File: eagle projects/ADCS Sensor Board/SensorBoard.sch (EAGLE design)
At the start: 129 parts, among them Q3 CSTCR4M00G15L99, Q5 32.768kHz, U10 LMV321, U2 ADS7841E_2K5, U3 LMV321, U5 ADS7841E_2K5, U6 REF194GSZ-REEL7, U7 TLV9054IDR, U8 LMV321

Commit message: Buncha layout done
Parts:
- removed C40: 9.1p, rcl:C-EUC0603
- removed C41, C43, C45, C46, C53, C54: 0.1u, rcl:C-EUC0603
- removed C42, C44: 1u, rcl:C-EUC0603
- removed R53, R57, R58: 5.1M, rcl:R-US_R0603
- removed R54, R55: 698k, rcl:R-US_R0603
- removed R59, R60: 10k, rcl:R-US_R0402
- removed R67, R68: 5.6k, rcl:R-US_R0805
- removed R69, R70: 1k, rcl:R-US_R0805
- removed R71, R72: 1.37M, rcl:R-US_R0805
- removed U$11: HMC1053, my_library:HMC1053
- removed U$14: LM20BIM7X_NOPB, my_library:LM20BIM7X_NOPB
- removed U$3: MTI-1, my_library:MTI-1
- removed U$7, U$9: BSS138PS,115, my_library:BSS138PS,115
- removed U10: LMV321, my_library:LMV321
- added A1: HMC1053PA0242, my_library:HMC1053PA0242
- added C13, C19, C23, C30: 0.1u, rcl:C-EUC0603
- added C20, C24, C27: 1n, rcl:C-EUC0805
- added C28: 470n, rcl:C-EUC0805
- added C29: 4.7u, rcl:C-EUC0603
- added J6: MTI-1_8428-11B1-RK-TP, my_library:MTI-1_8428-11B1-RK-TP
- added R1: 0R, rcl:R-US_R0402
- added R15: 5.1M, resistor:R-US_R1206
- added R16, R9: 5.6k, rcl:R-US_R0805
- added R2: 47k, rcl:R-US_R0402
- added R27: 27R, rcl:R-US_R0805
- added R28: 10k, rcl:R-US_R0402
- added R3: 1k4, rcl:R-US_R0402
- added R35: 698k, rcl:R-US_R0603
- added R4: 100R, rcl:R-US_R0402
- added R5: 1M, rcl:R-US_R0402
- added R6: 200R, resistor:R-US_R1206
- added R7: 1k, rcl:R-US_R0805
- added U4: LMV321, my_library:LMV321
- added U9: ADS7841E_2K5, my_library:ADS7841E_2K5
- added Y1: 32.768kHz, my_library:MS3V-T1R
- added Y2: CSTCR4M00G15L99, my_library:CSTCR4M00G15L996M00G53Z
- C14: value 470n -> 0.1u; device rcl:C-EUC0805 -> rcl:C-EUC0603
- C17, C25: value 1n -> 0.1u; device rcl:C-EUC0805 -> rcl:C-EUC0603
- C21: device rcl:C-EUC0805 -> resistor:C-EUC1206
- C31: value 1n -> 9.1p; device resistor:C-EUC1206 -> rcl:C-EUC0603
- C32, C33: value 0.1u -> 9.1p
- C34: value 0.1u -> 1u
- C36: value 4.7u -> 1u
- C38, C39: value 9.1p -> 0.1u
- JP1: value 5034801000 -> (none); device my_library:5034801000 -> jumper:JP1Q
- JP2: device jumper:JP1Q -> pinhead:PINHD-2X5
- JP3, JP4: value 5034801000 -> (none); device my_library:5034801000 -> pinhead:PINHD-2X5
- JP5: value 5034801000 -> (none); device my_library:5034801000 -> pinhead:PINHD-1X4
- Q3: value CSTCR4M00G15L99 -> BSS138PS,115; device murata:MURATA-FILTER_CSTCR6M00G53Z -> my_library:BSS138PS,115
- Q5: value 32.768kHz -> BSS138PS,115; device microcrystal:MS3V-T1R -> my_library:BSS138PS,115
- R10: value 47k -> 5.6k; device rcl:R-US_R0402 -> rcl:R-US_R0805
- R11: value 0R -> 1.37M; device rcl:R-US_R0402 -> rcl:R-US_R0805
- R12, R18, R19: value 10k -> 1.37M; device rcl:R-US_R0402 -> rcl:R-US_R0805
- R13, R14, R20: value 10k -> 1k; device rcl:R-US_R0402 -> rcl:R-US_R0805
- R17: value 100R -> 5.6k; device rcl:R-US_R0402 -> rcl:R-US_R0805
- R21: value 5.6k -> 1k
- R23: value 1k -> 5.6k
- R24: value 1k -> 1.37M
- R26: value 1.37M -> 5.1M; device rcl:R-US_R0805 -> resistor:R-US_R1206
- R29: value 1k4 -> 10k
- R30: device resistor:R-US_R1206 -> rcl:R-US_R0603
- R31: value 200R -> 10k; device resistor:R-US_R1206 -> rcl:R-US_R0402
- R32: value 5.1M -> 10k; device resistor:R-US_R1206 -> rcl:R-US_R0402
- R33: value 1M -> 10k
- R36: value 5.6k -> 698k; device rcl:R-US_R0805 -> rcl:R-US_R0603
- R38: value 5.6k -> 10k; device rcl:R-US_R0805 -> rcl:R-US_R0402
- R39: value 1k -> 10k; device rcl:R-US_R0805 -> rcl:R-US_R0402
- R40: value 1k -> 5.1M; device rcl:R-US_R0805 -> rcl:R-US_R0603
- R41: value 1.37M -> 5.1M; device rcl:R-US_R0805 -> rcl:R-US_R0603
- R42: value 1.37M -> 10k; device rcl:R-US_R0805 -> rcl:R-US_R0402
- R43, R45, R46: value 13.7k -> 10k; device rcl:R-US_R0603 -> rcl:R-US_R0402
- R44: value 13.7k -> 5.1M
- R49: value 5.1M -> 13.7k
- R50, R51, R52: value 10k -> 13.7k; device rcl:R-US_R0402 -> rcl:R-US_R0603
- R8: value 27R -> 1k
- U2: value ADS7841E_2K5 -> LMV321; device my_library:ADS7841E_2K5 -> my_library:LMV321
- U3: value LMV321 -> ADS7841E_2K5; device my_library:LMV321 -> my_library:ADS7841E_2K5
- U5: value ADS7841E_2K5 -> LM20BIM7X_NOPB; device my_library:ADS7841E_2K5 -> my_library:LM20BIM7X_NOPB
- U6: value REF194GSZ-REEL7 -> LMV321; device my_library:REF194GSZ-REEL7 -> my_library:LMV321
- U8: value LMV321 -> REF194GSZ-REEL7; device my_library:LMV321 -> my_library:REF194GSZ-REEL7
- renumbered C47 to C35, C48 to C7, C49 to C11, C50 to C8, C51 to C10, C52 to C6, C55 to C15, C56 to C12, C57 to C16, C58 to C3, C59 to C5, C60 to C4, C61 to C1, C62 to C2, C63 to C9, D4 to D1, D5 to D2, D6 to D3, R61 to R34, S4 to S1, S6 to S2, U$1 to U1, U$10 to Q2, U$13 to Q6, U$17 to Q4, U$2 to J5
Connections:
- removed net N$10: JP5.7
- removed net N$11: JP3.7
- removed net N$13: JP3.8
- removed net N$15: JP3.9
- removed net N$16: JP3.10
- removed net N$17: JP5.8
- removed net N$18: JP5.9
- removed net N$19: JP5.10
- removed net N$3: JP5.3
- removed net N$4: JP5.4
- removed net N$5: JP5.5
- removed net N$6: JP1.6
- removed net N$8: JP1.7
- removed net N$9: JP5.6
- removed net P6.4: U1.P6.4/CB4/A4
- new net INIT_EPS_BURN_WIRE: JP5.3, U1.P4.7/PM_NONE
- net !CS!_HMC1053: now also U3.!CS; no longer U$3.SPI_!CS, U2.!CS
- net !CS!_MTI: now also J6.SPI_!CS
- net !CS!_SUN_X+: now also JP2.10; no longer JP1.1
- net !CS!_SUN_X-: now also JP2.8; no longer JP1.2
- net !CS!_SUN_Y+: now also JP2.4; no longer JP1.4
- net !CS!_SUN_Y-: now also JP2.2; no longer JP1.5
- net !CS!_SUN_Z-: now also JP2.6, R43.1; no longer JP1.3, R51.1
- net +3V3: now also A1.VB, C14.1, C17.1, C19.1, C23.1, C25.2, J6.PSEL1, J6.VDDIO, JP5.2, Q3.G1, Q3.G2, Q5.G1, Q5.G2, R1.2, R13.1, R2.2, R20.1, R27.1, R28.1, R29.1, R32.2, R38.1, R42.2, R43.2, R6.2, R7.1, U2.V+, U3.!SHDN, U3.VCC+, U3.VCC+_2, U3.VREF, U4.V+, U5.V+, U6.V+; no longer C32.1, C34.2, C41.1, C53.1, C54.1, R10.2, R11.2, R12.1, R13.2, R18.1, R19.2, R23.1, R50.1, R51.2, R59.1, R60.2, R69.1, R8.1, U$11.VB, U$14.V+, U$3.PSEL1, U$3.VDDIO, U$7.G1, U$7.G2, U$9.G1, U$9.G2, U10.V+, U2.!SHDN, U2.VCC+, U2.VCC+_2, U2.VREF, U3.V+, U8.V+
- net +4V5: now also C34.1, C39.1, U8.OUTPUT, U9.VREF; no longer C42.1, C43.1, U5.VREF, U6.OUTPUT
- net +5V: now also C29.1, C30.1, C38.1, JP5.1, R33.2, R45.2, R47.2, R49.2, R51.2, U8.!SLEEP, U8.VS, U9.!SHDN, U9.VCC+, U9.VCC+_2; no longer C44.1, C45.1, C46.1, R14.2, R20.2, R44.2, R48.2, R52.2, U5.!SHDN, U5.VCC+, U5.VCC+_2, U6.!SLEEP, U6.VS
- net 0_DEGREES: now also C33.2, R37.2, U9.CH0; no longer C40.2, R55.2, U5.CH0
- net 120_DEGREES: now also C32.2, R36.2, U9.CH1; no longer C39.2, R54.2, U5.CH1
- net 240_DEGREES: now also C31.2, R35.2, U9.CH2; no longer C38.2, R37.2, U5.CH2
- net 5V_!CS!_SUN_Z-: now also R46.1, U9.!CS; no longer R52.1, U5.!CS
- net 5V_SPI_CLK: now also Q3.D2, R33.1, U9.DCLK; no longer R14.1, U$7.D2, U5.DCLK
- net 5V_SPI_MISO: now also U9.DOUT; no longer U5.DOUT
- net 5V_SPI_MOSI: now also Q5.D2, R45.1, U9.DIN; no longer R20.1, U$9.D2, U5.DIN
- net ACT_BRD_3V_PRESENT: now also JP4.7; no longer JP4.3, JP5.1
- net ACT_BRD_5V_PRESENT: now also JP4.5; no longer JP4.4, JP5.2
- net AVCC1: now also R1.1; no longer R11.1
- net BRD_TEMP_MEAS: now also U3.CH3, U5.VO; no longer U$14.VO, U2.CH3
- net B_MEAS_X: now also C24.2, R19.1, U3.CH2, U4.OUT; no longer C21.2, R41.1, U2.CH2, U8.OUT
- net B_MEAS_Y: now also C20.2, R12.1, U2.OUT, U3.CH1; no longer C17.2, R25.1, U2.CH1, U3.OUT
- net B_MEAS_Z: now also C27.2, R25.1, U3.CH0, U6.OUT; no longer C25.2, R71.1, U10.OUT, U2.CH0
- net GND: now also A1.GND(A), A1.GND(B), A1.GND(C), A1.S/R-(A,B,C), C13.1, C14.2, C17.2, C19.2, C23.2, C25.1, C28.1, C29.2, C30.2, C34.2, C38.2, C39.2, J6.GND_1, J6.GND_2, J6.GND_3, J6.GND_4, JP5.4, R14.2, R15.1, R21.2, R26.1, R41.1, R44.1, R48.1, R5.1, R50.1, R52.1, R8.2, U2.V-, U3.COM, U3.GND, U3.MODE, U4.V-, U5.GND_1, U5.GND_2, U6.V-, U8.GND, U9.COM, U9.GND, U9.MODE, Y1.GND, Y2.2; no longer C14.1, C32.2, C33.1, C34.1, C41.2, C42.2, C43.2, C44.2, C45.2, C46.2, C53.2, C54.2, JP1.SHIELD, JP3.SHIELD, JP4.SHIELD, JP5.SHIELD, Q3.2, Q5.GND, R24.2, R32.1, R33.1, R43.1, R45.1, R47.1, R49.1, R53.2, R57.1, R58.1, R70.2, U$11.GND(A), U$11.GND(B), U$11.GND(C), U$11.S/R-(A,B,C), U$14.GND_1, U$14.GND_2, U$3.GND_1, U$3.GND_2, U$3.GND_3, U$3.GND_4, U10.V-, U2.COM, U2.GND, U2.MODE, U3.V-, U5.COM, U5.GND, U5.MODE, U6.GND, U8.V-
- net HMC1053_RESET: now also U1.P6.4/CB4/A4
- net IN2+BIAS: now also R47.1, R48.2; no longer R43.2, R44.1
- net IN3+BIAS: now also R49.1, R50.2; no longer R45.2, R46.1
- net IN4+BIAS: now also R51.1, R52.2; no longer R47.2, R48.1
- net MAG_Y_FIN: now also JP3.6; no longer JP3.3
- net MAG_Y_RIN: now also JP3.8; no longer JP3.4
- net MAG_Z_FIN: now also JP3.10, JP3.2; no longer JP3.1, JP3.5
- net MAG_Z_RIN: now also JP3.4, JP3.9; no longer JP3.2, JP3.6
- net MTI_DRDY: now also J6.DRDY/RE/CTS; no longer U$3.DRDY/RE/CTS
- net N$12: now also R4.1; no longer R17.1
- net N$14: now also Q3.S1, Q3.S2, R28.2; no longer R12.2, U$7.S1, U$7.S2
- net N$20: now also R11.1, R7.2, R8.1; no longer R23.2, R24.1, R26.1
- net N$21: now also C20.1, R10.1, R12.2, U2.-; no longer C17.1, R22.1, R25.2, U3.-
- net N$23: now also R11.2, R9.1, U2.+; no longer R21.1, R26.2, U3.+
- net N$26: now also R30.2; no longer R49.2
- net N$27: now also R40.1; no longer R53.1
- net N$28: now also C31.1, R35.1; no longer C38.1, R37.1
- net N$30: now also Q5.S1, Q5.S2, R38.2; no longer R18.2, U$9.S1, U$9.S2
- net N$31: now also C32.1, R36.1; no longer C39.1, R54.1
- net N$32: now also C33.1, R37.1; no longer C40.1, R55.1
- net N$33: now also U8.TP_2; no longer U6.TP_2
- net N$34: now also U8.TP_1; no longer U6.TP_1
- net N$35: now also C21.2, JP1.2; no longer C31.2, JP2.2
- net N$36: now also A1.OFF+(A,B,C), A1.OFF-(A,B), A1.OFF-(C), R15.2; no longer R30.2, U$11.OFF+(A,B,C), U$11.OFF-(A,B), U$11.OFF-(C)
- net N$37: now also A1.S/R+(A,B), A1.S/R+(C), JP1.1; no longer JP2.1, U$11.S/R+(A,B), U$11.S/R+(C)
- net N$38: now also C21.1; no longer C31.1
- net N$39: now also C13.2, R6.1; no longer C33.2, R31.1
- net N$40: now also R26.2, U5.NC; no longer R32.2, U$14.NC
- net N$41: now also R41.2, U8.NC_1; no longer R57.2, U6.NC_1
- net N$42: now also R39.2; no longer R50.2
- net N$43: now also R44.2, U8.NC_2; no longer R58.2, U6.NC_2
- net N$48: now also R29.2; no longer R59.2
- net N$49: now also R13.2, R14.1, R18.1; no longer R39.2, R40.1, R42.1
- net N$50: now also C24.1, R17.1, R19.2, U4.-; no longer C21.1, R38.1, R41.2, U8.-
- net N$52: now also R16.1, R18.2, U4.+; no longer R36.1, R42.2, U8.+
- net N$59: now also R20.2, R21.1, R24.1; no longer R69.2, R70.1, R72.1
- net N$60: now also C27.1, R23.1, R25.2, U6.-; no longer C25.1, R68.1, R71.2, U10.-
- net N$62: now also R22.1, R24.2, U6.+; no longer R67.1, R72.2, U10.+
- net N$7: now also C28.2, J6.VDDA, R27.2; no longer C14.2, R8.2, U$3.VDDA
- net OUT_A_N: now also A1.OUT-(A), R9.2; no longer R21.2, U$11.OUT-(A)
- net OUT_A_P: now also A1.OUT+(A), R10.2; no longer R22.2, U$11.OUT+(A)
- net OUT_B_N: now also A1.OUT-(B), R16.2; no longer R36.2, U$11.OUT-(B)
- net OUT_B_P: now also A1.OUT+(B), R17.2; no longer R38.2, U$11.OUT+(B)
- net OUT_C_N: now also A1.OUT-(C), R22.2; no longer R67.2, U$11.OUT-(C)
- net OUT_C_P: now also A1.OUT+(C), R23.2; no longer R68.2, U$11.OUT+(C)
- net P5.2/XT2IN1: now also Y2.3; no longer Q3.3
- net P5.3/XT2OUT1: now also Y2.1; no longer Q3.1
- net P5.4/XIN1: now also Y1.2; no longer Q5.2
- net P5.5/XOUT1: now also Y1.1; no longer Q5.1
- net RST/SBWTDIO: now also R2.1; no longer R10.1
- net SEN_BRD_3V_PRESENT: now also JP4.3; no longer JP4.5
- net SEN_BRD_5V_PRESENT: now also JP4.1; no longer JP4.6
- net TARGET_DP: now also R3.2; no longer R29.2
- net TARGET_PUR: now also R3.1, R4.2, R5.2; no longer R17.2, R29.1, R33.2
- net UCA0RXD: now also JP4.10; no longer JP4.1
- net UCA0TXD: now also JP4.8; no longer JP4.2
- net UCB0_SPI_CLK: now also J6.SPI_SCK, JP2.1, Q3.D1, R31.1, U3.DCLK; no longer JP1.10, R13.1, U$3.SPI_SCK, U$7.D1, U2.DCLK
- net UCB0_SPI_MISO: now also J6.SPI_MISO, JP2.3, R32.1, U3.DOUT; no longer JP1.9, R60.1, U$3.SPI_MISO, U2.DOUT
- net UCB0_SPI_MOSI: now also J6.SPI_MOSI, JP2.5, Q5.D1, R42.1, U3.DIN; no longer JP1.8, R19.1, U$3.SPI_MOSI, U$9.D1, U2.DIN
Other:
- note added: "I think TARGET_DP is uneccessary"
- note removed: "Change resistors to american symbols"

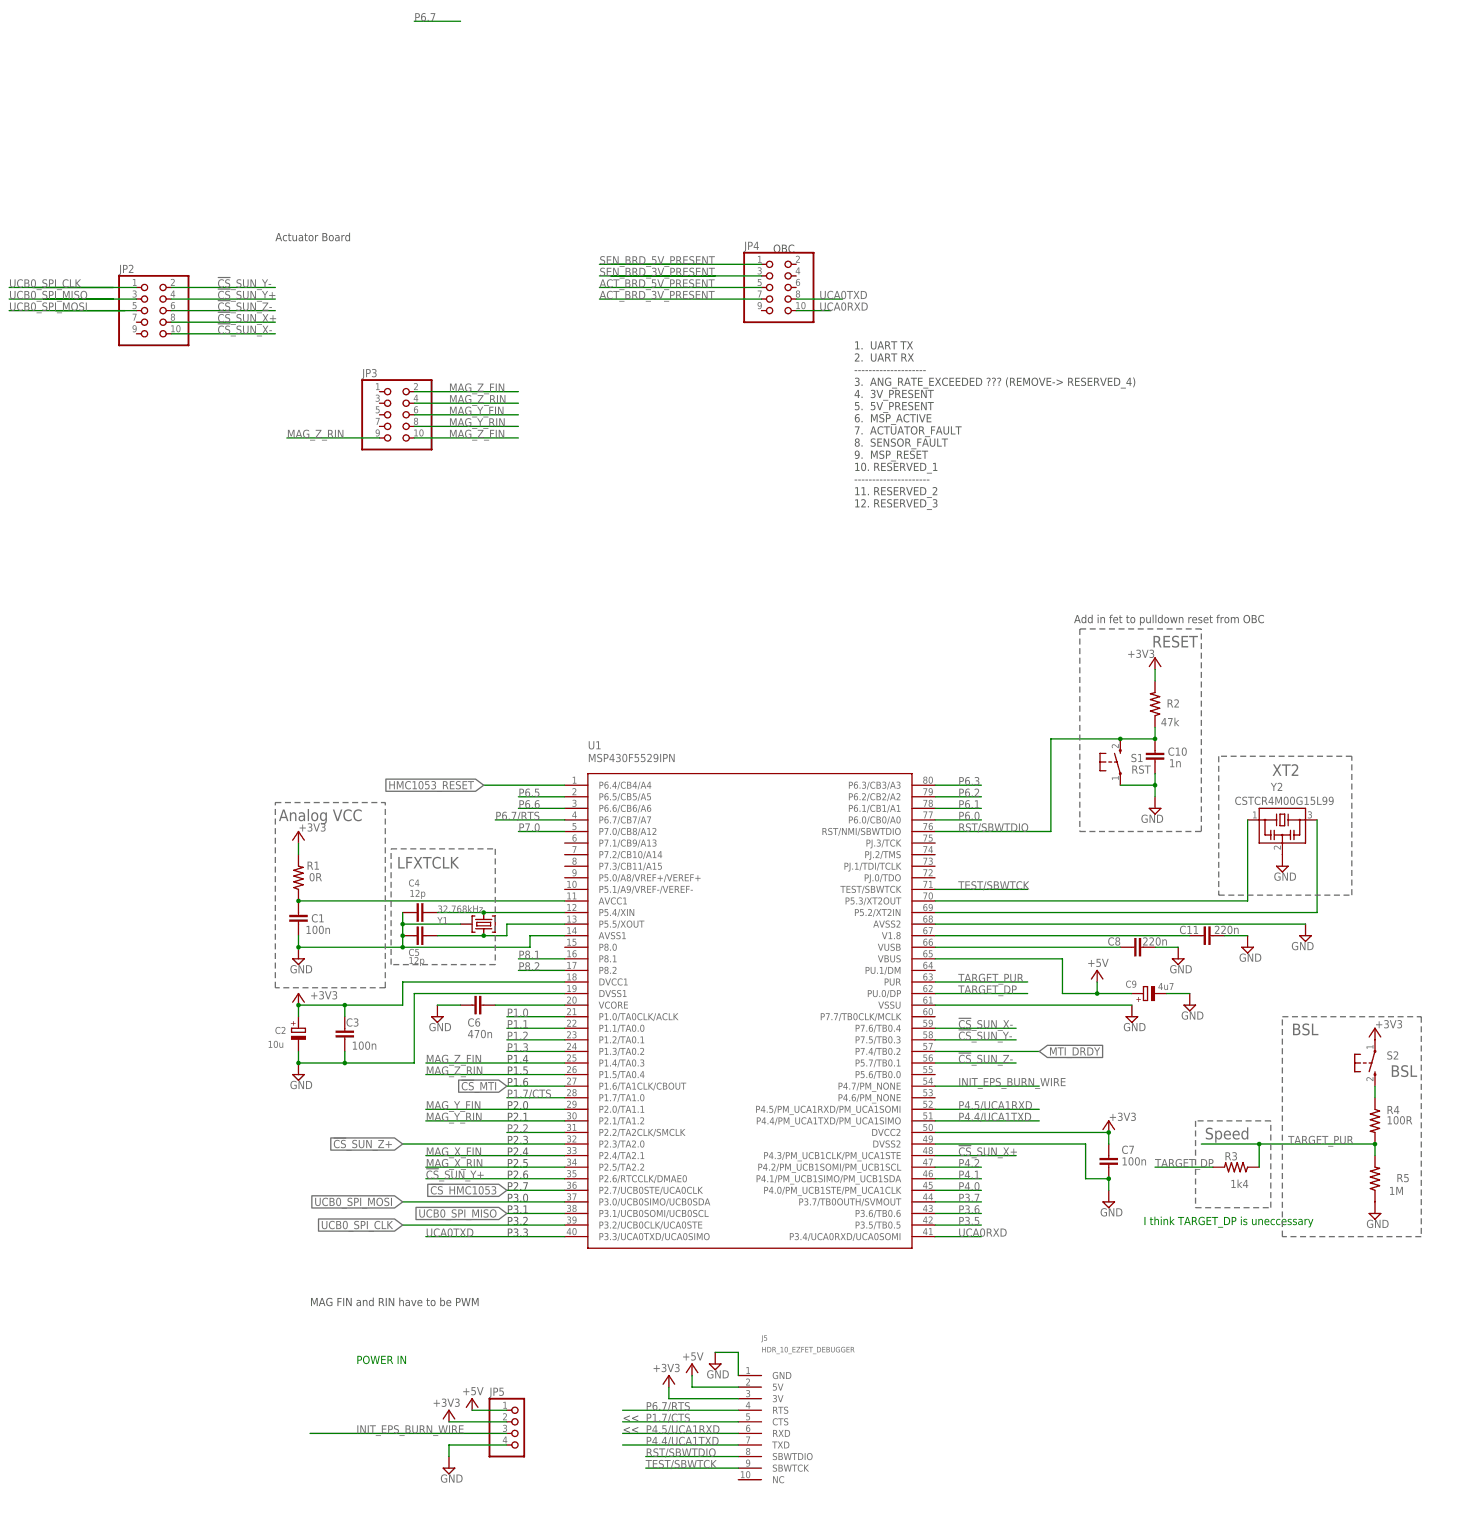
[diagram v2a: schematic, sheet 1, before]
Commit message: Board update commit before removing Z+ sunsensor from layout
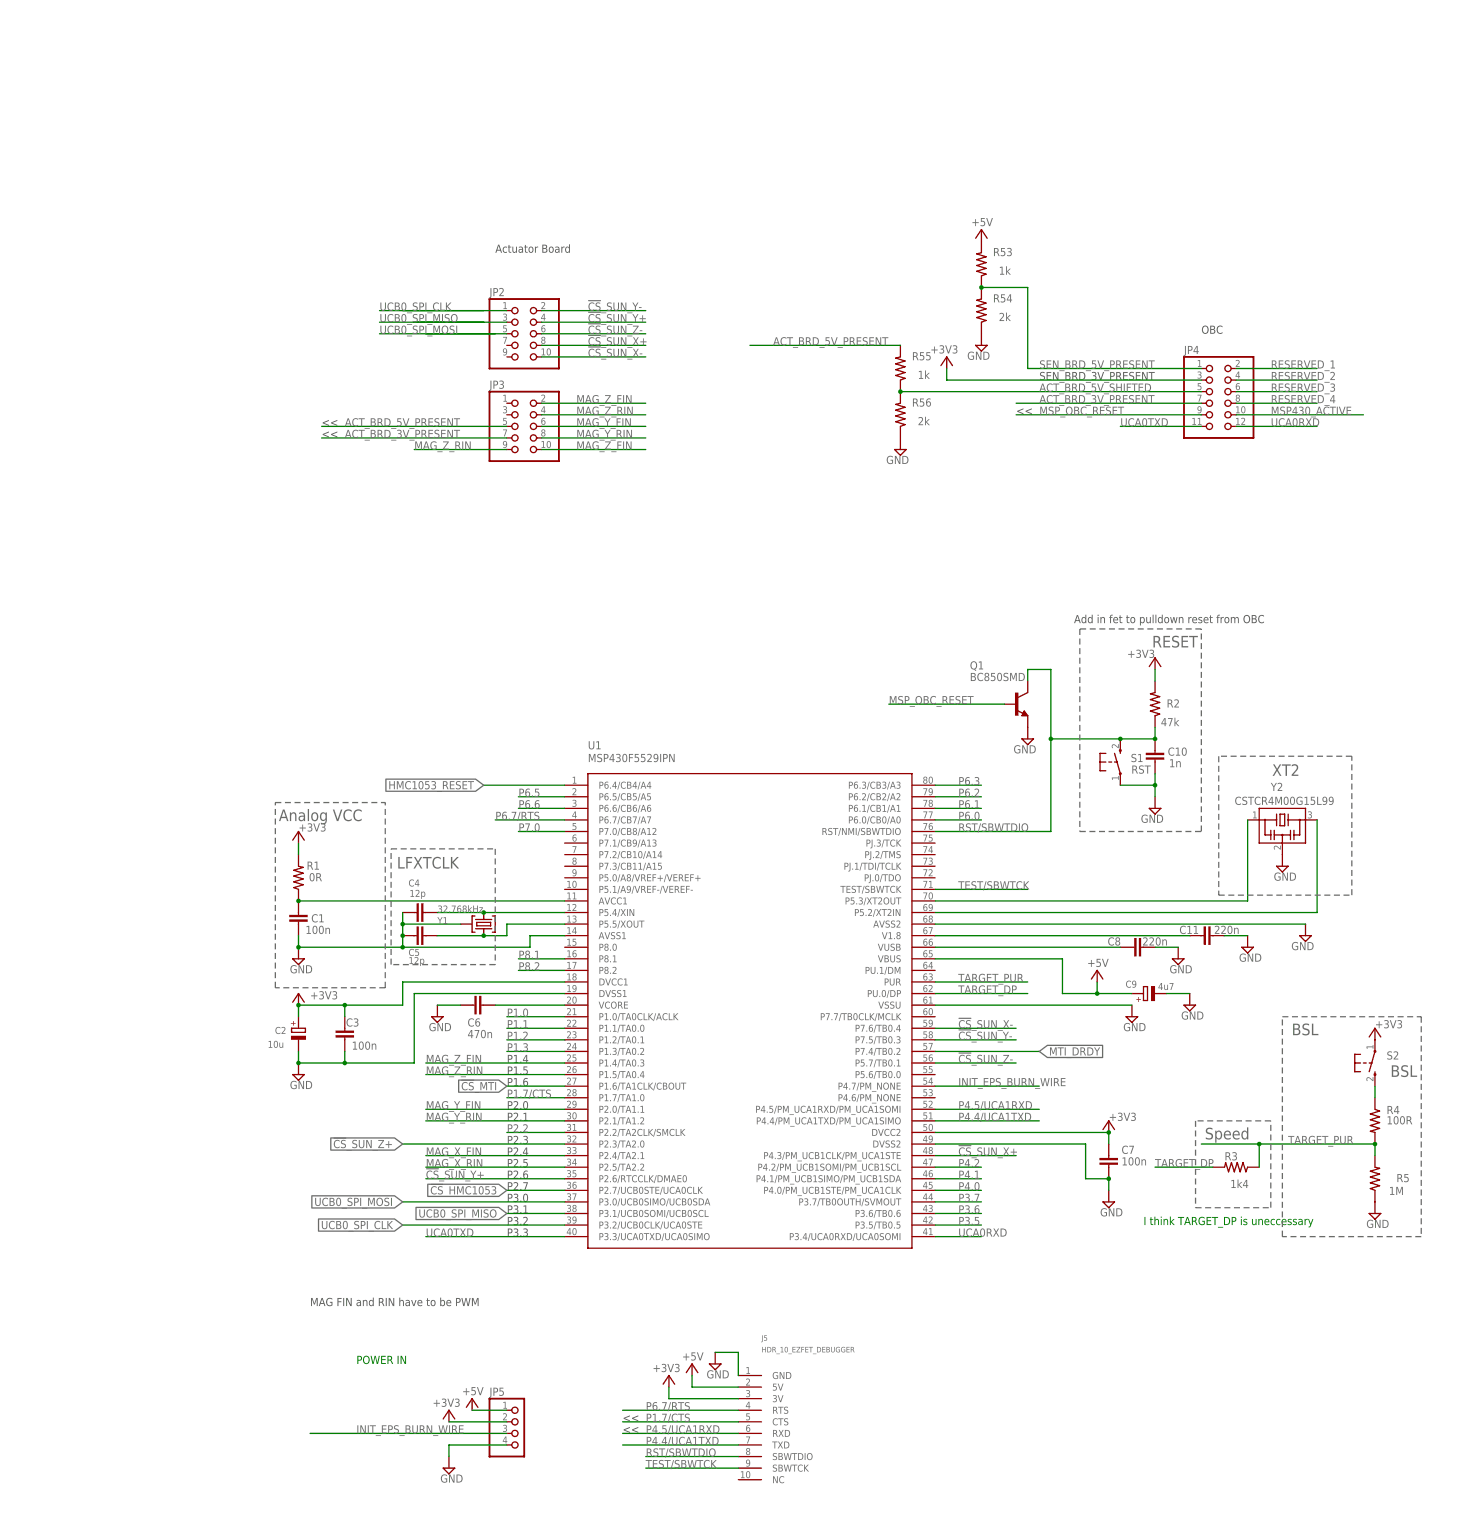
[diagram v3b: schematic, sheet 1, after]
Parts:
- added Q1: BC850SMD, transistor-npn:BC850SMD
- added R53, R55: 1k, rcl:R-US_R0402
- added R54, R56: 2k, rcl:R-US_R0402
- JP4: device pinhead:PINHD-2X5 -> pinhead:PINHD-2X6
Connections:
- removed net SEN_BRD_3V_PRESENT: JP4.3
- new net ACT_BRD_5V_SHIFTED: JP4.5, R55.1, R56.2
- new net MSP430_ACTIVE: JP4.10
- new net MSP_OBC_RESET: JP4.9
- new net N$1: Q1.B
- new net RESERVED_1: JP4.2
- new net RESERVED_2: JP4.4
- new net RESERVED_3: JP4.6
- new net RESERVED_4: JP4.8
- net +3V3: now also JP4.3
- net +5V: now also R53.2
- net ACT_BRD_3V_PRESENT: now also JP3.7
- net ACT_BRD_5V_PRESENT: now also JP3.5, R55.2; no longer JP4.5
- net GND: now also Q1.E, R54.1, R56.1
- net RST/SBWTDIO: now also Q1.C
- net SEN_BRD_5V_PRESENT: now also R53.1, R54.2
- net UCA0RXD: now also JP4.12; no longer JP4.10
- net UCA0TXD: now also JP4.11; no longer JP4.8
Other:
- note added: "SEN_BRD_3V_PRESENT"
- note removed: "1. UART TX 2. UART RX -------------------- 3. ANG_RATE_EXCEEDED ??? (REMOVE-> RESERVED_4) 4. 3V_PRESENT 5. 5V_PRESENT 6. MSP_ACTIVE 7. ACTUATOR_FAULT 8. SENSOR_FAULT 9. MSP_RESET 10. RESERVED_1 --------------------- 11. RESERVED_2 12. RESERVED_3"
- moved on the sheet: JP2, JP3

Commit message: Added files for Sunsensor Boards
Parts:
- removed C29: 4.7u, rcl:C-EUC0603
- removed C30, C37, C38, C39: 0.1u, rcl:C-EUC0603
- removed C31, C32, C33: 9.1p, rcl:C-EUC0603
- removed C34, C35, C36: 1u, rcl:C-EUC0603
- removed D1, D2, D3: SFH2430, my_library:SFH2430
- removed Q3, Q4, Q5, Q6: BSS138PS,115, my_library:BSS138PS,115
- removed R28, R29, R31, R32, R33, R34, R38, R39, R42, R43, R45, R46: 10k, rcl:R-US_R0402
- removed R30, R40, R41, R44: 5.1M, rcl:R-US_R0603
- removed R35, R36, R37: 698k, rcl:R-US_R0603
- removed R47, R48, R49, R50, R51, R52: 13.7k, rcl:R-US_R0603
- removed TP4, TP5: TPB1,27, testpad:TPB1,27
- removed U7: TLV9054IDR, my_library:TLV9054IDR
- removed U8: REF194GSZ-REEL7, my_library:REF194GSZ-REEL7
- removed U9: ADS7841E_2K5, my_library:ADS7841E_2K5
- added A2, A3: ARDUCAM_OV5642, my_library:ARDUCAM_OV5642
- C1, C10, C11, C3, C4, C5, C6, C7, C8: device rcl:C-EUCM0402 -> rcl:C-EUC0402
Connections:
- removed net +4V5: C34.1, C39.1, U8.OUTPUT, U9.VREF
- removed net 0_DEGREES: C33.2, R37.2, U7.OUT2, U9.CH0
- removed net 120_DEGREES: C32.2, R36.2, U7.OUT3, U9.CH1
- removed net 240_DEGREES: C31.2, R35.2, U7.OUT4, U9.CH2
- removed net 5V_!CS!_SUN_Z-: Q6.D2, R46.1, U9.!CS
- removed net 5V_SPI_CLK: Q3.D2, R33.1, U9.DCLK
- removed net 5V_SPI_MISO: Q4.D2, R34.1, U9.DOUT
- removed net 5V_SPI_MOSI: Q5.D2, R45.1, U9.DIN
- removed net IN2+BIAS: R47.1, R48.2, U7.IN2+
- removed net IN3+BIAS: R49.1, R50.2, U7.IN3+
- removed net IN4+BIAS: R51.1, R52.2, U7.IN4+
- removed net N$14: Q3.S1, Q3.S2, R28.2
- removed net N$26: R30.2, U7.IN1+, U7.IN1-
- removed net N$27: R40.1, U7.OUT1
- removed net N$28: C31.1, D3.C, R35.1, U7.IN4-
- removed net N$30: Q5.S1, Q5.S2, R38.2
- removed net N$31: C32.1, D2.C, R36.1, U7.IN3-
- removed net N$32: C33.1, D1.C, R37.1, U7.IN2-
- removed net N$33: TP5.TP, U8.TP_2
- removed net N$34: TP4.TP, U8.TP_1
- removed net N$41: R41.2, U8.NC_1
- removed net N$42: Q6.S1, Q6.S2, R39.2
- removed net N$43: R44.2, U8.NC_2
- removed net N$48: Q4.S1, Q4.S2, R29.2
- new net !CS!_CAM_A: A2.CS
- new net !CS!_CAM_B: A3.CS
- new net N$17: A3.+5V
- new net PAYLOAD_MISO: A2.MISO, A3.MISO
- new net PAYLOAD_MOSI: A2.MOSI, A3.MOSI
- new net PAYLOAD_SCL: A2.SCL, A3.SCL
- new net PAYLOAD_SCLK: A2.SCLK, A3.SCLK
- new net PAYLOAD_SDA: A2.SDA, A3.SDA
- net !CS!_SUN_Z-: no longer Q6.D1, R43.1
- net +3V3: no longer Q3.G1, Q3.G2, Q4.G1, Q4.G2, Q5.G1, Q5.G2, Q6.G1, Q6.G2, R28.1, R29.1, R31.2, R32.2, R38.1, R39.1, R42.2, R43.2
- net +5V: now also A2.+5V; no longer C29.1, C30.1, C35.1, C36.1, C37.1, C38.1, R33.2, R34.2, R45.2, R46.2, R47.2, R49.2, R51.2, U7.V+, U8.!SLEEP, U8.VS, U9.!SHDN, U9.VCC+, U9.VCC+_2
- net BRD_TEMP_MEAS: now also U3.CH0; no longer U3.CH3
- net B_MEAS_X: now also U3.CH3; no longer U3.CH2
- net B_MEAS_Y: now also U3.CH2; no longer U3.CH1
- net B_MEAS_Z: now also U3.CH1; no longer U3.CH0
- net GND: now also A2.GND, A3.GND; no longer C29.2, C30.2, C34.2, C35.2, C36.2, C37.2, C38.2, C39.2, D1.A, D2.A, D3.A, R30.1, R40.2, R41.1, R44.1, R48.1, R50.1, R52.1, U7.V-, U8.GND, U9.COM, U9.GND, U9.MODE
- net UCB0_SPI_CLK: no longer Q3.D1, R31.1
- net UCB0_SPI_MISO: no longer Q4.D1, R32.1
- net UCB0_SPI_MOSI: no longer Q5.D1, R42.1
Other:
- note added: "Replace MTI-1 IMU with new 3-axis gyroscope in Rev B"
- note removed: "Replace MTI-1 IMU with new 3-axis gyroscope"
